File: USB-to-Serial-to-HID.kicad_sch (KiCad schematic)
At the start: 11 parts, among them J2 USB4520-03-1-A, J3 48037-2200, U1 CH340E, U2 CH9329

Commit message: Move to CH340C
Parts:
- removed U1: CH340E, Package_SO:MSOP-10_3x3mm_P0.5mm, symbol Interface_USB:CH340E
- added C6: 100nF, Capacitor_SMD:C_0805_2012Metric_Pad1.18x1.45mm_HandSolder, symbol Device:C
- added JP1: TX, TestPoint:TestPoint_2Pads_Pitch2.54mm_Drill0.8mm, symbol Jumper:SolderJumper_2_Bridged
- added JP2: RX, TestPoint:TestPoint_2Pads_Pitch2.54mm_Drill0.8mm, symbol Jumper:SolderJumper_2_Bridged
- added U1: CH340C, Package_SO:SOIC-16_3.9x9.9mm_P1.27mm, symbol Interface_USB:CH340C
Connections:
- net +5V: now also U1.16 (VCC)
- net DI+: now also U1.5 (UD+)
- net DI-: now also U1.6 (UD-)
- net GND: now also C6.1, U1.1 (GND)
- net CH340E_RX renamed CH340_RX
- net CH340_RX: now also JP2.1 (A), JP2.2 (B), U1.3 (RXD)
- net CH340E_TX renamed CH340_TX
- net CH340_TX: now also JP1.1 (A), JP1.2 (B), U1.2 (TXD)
- new net: C6.2, U1.4 (V3)
- no-connect marks 16 -> 19
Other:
- note added: "For Debug"
- note added: "Serial Test Points"

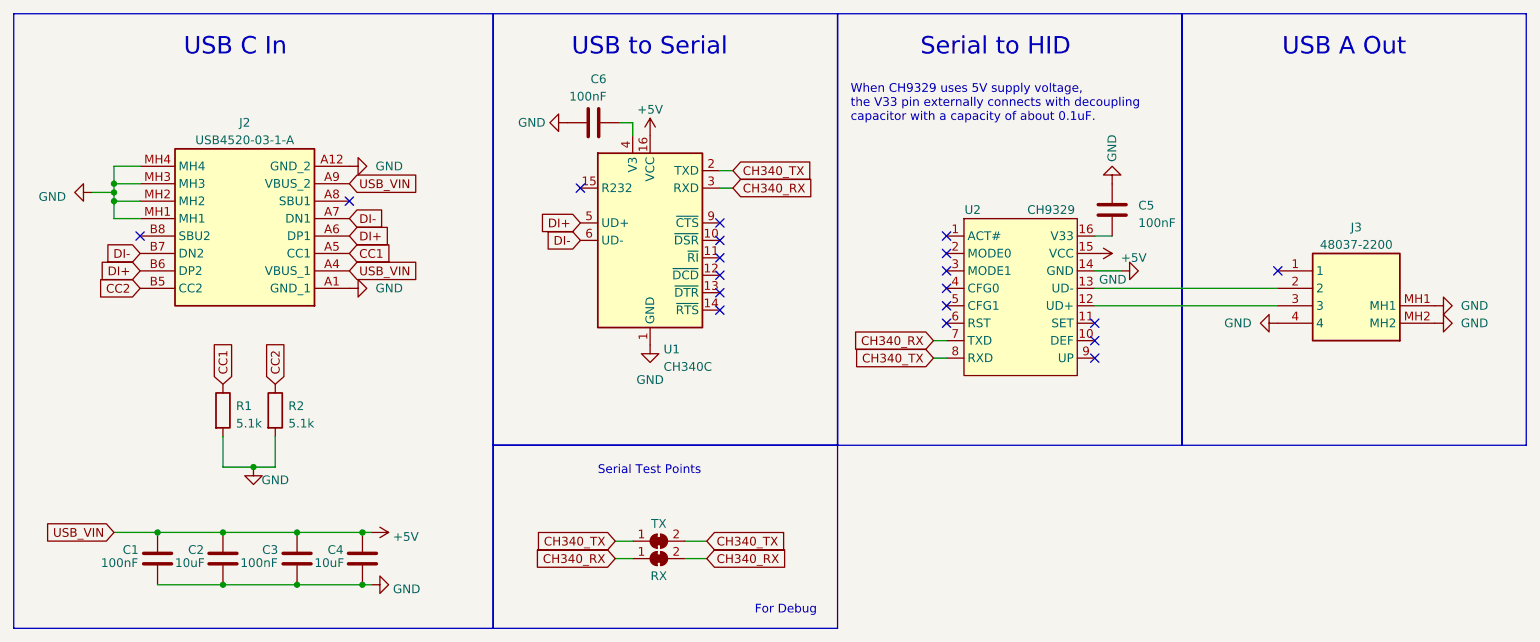
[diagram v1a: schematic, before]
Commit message: Update to use target 5V as well as host 5V
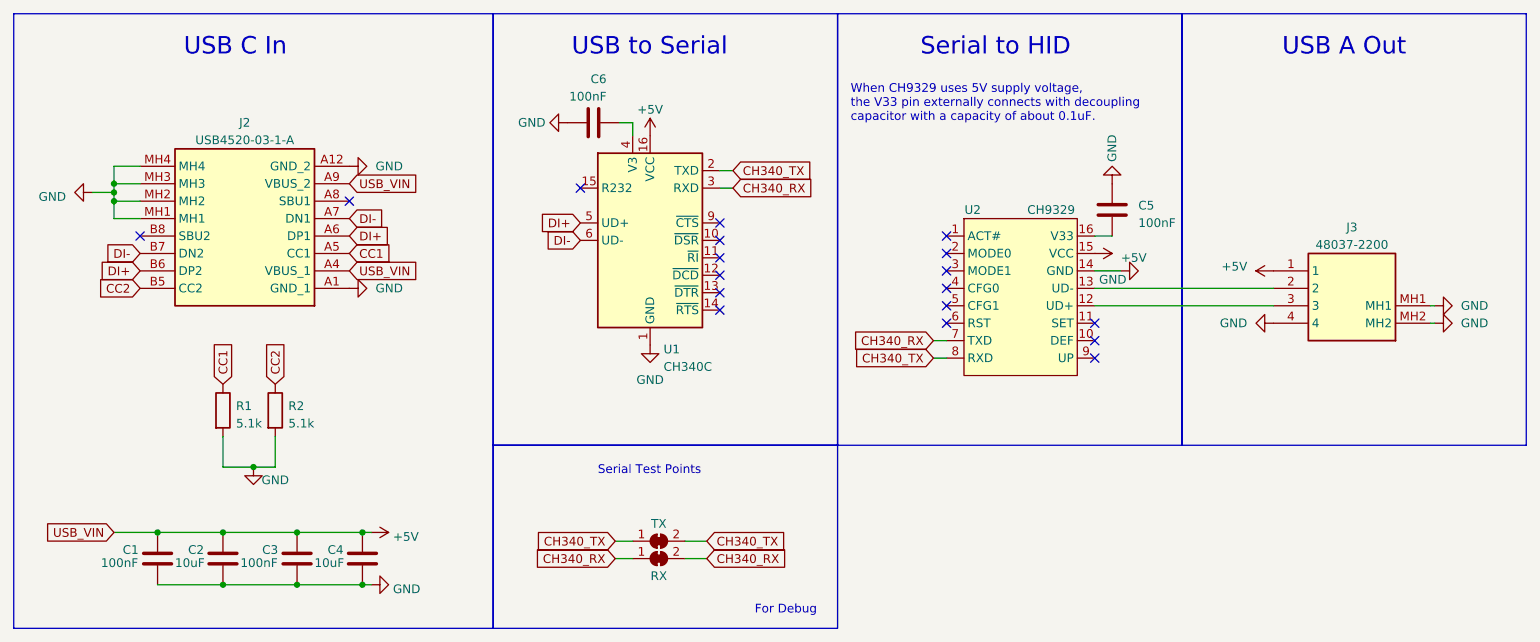
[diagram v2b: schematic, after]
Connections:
- net +5V: now also J3.1
- no-connect marks 19 -> 18
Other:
- moved on the sheet: J3
